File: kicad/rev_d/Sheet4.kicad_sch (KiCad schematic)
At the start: 22 parts, among them J2 JUMPER, J3 JUMPER, X7 DB15VGA, X8 PLB1-4I, X9 PLB1-2

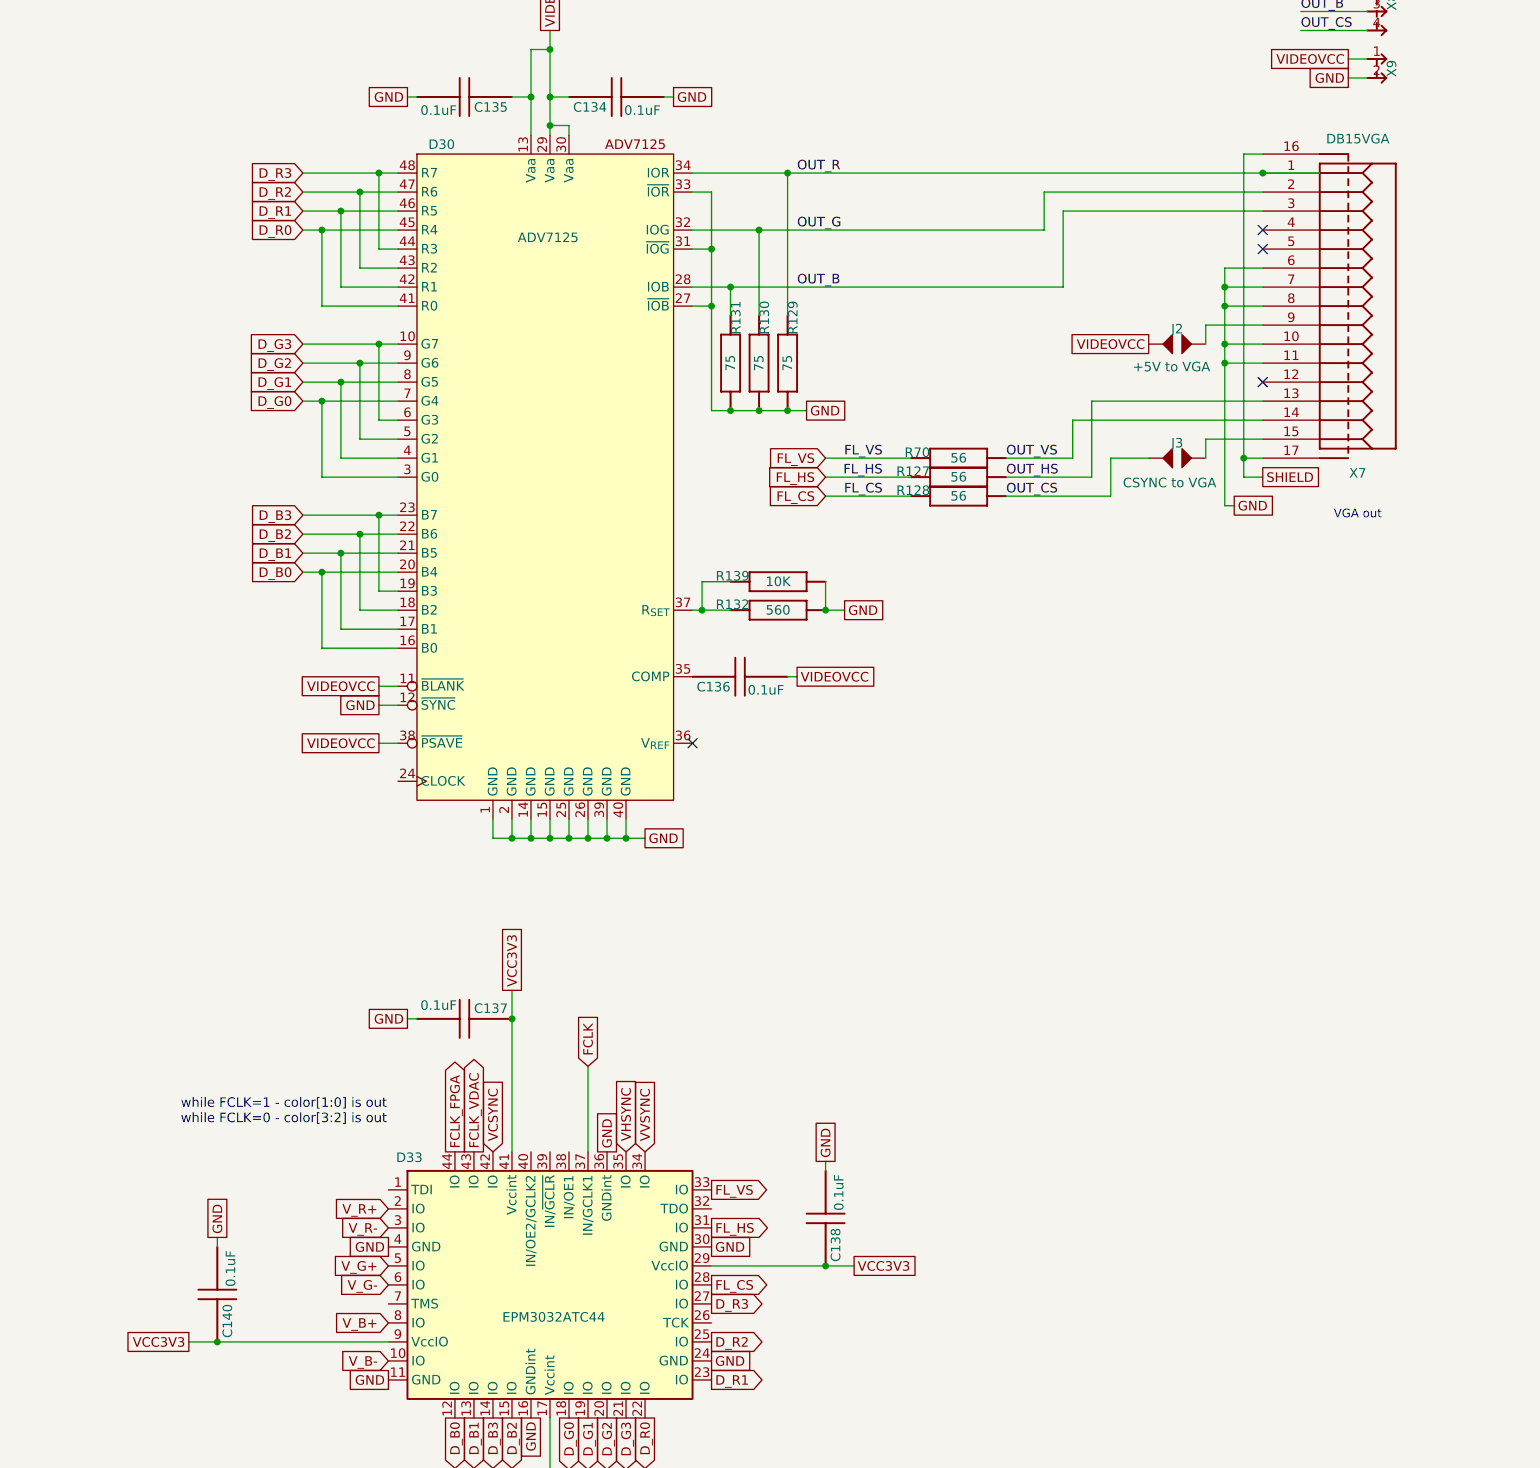
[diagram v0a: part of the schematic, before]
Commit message: pentevo: rev D: video output: remove 373/374 stuff (WIP); fix DA numbering issue
git-svn-id: svn://localhost/local-pentevo@1282 c6c76956-fad2-4150-a3a9-ea0a427205ba
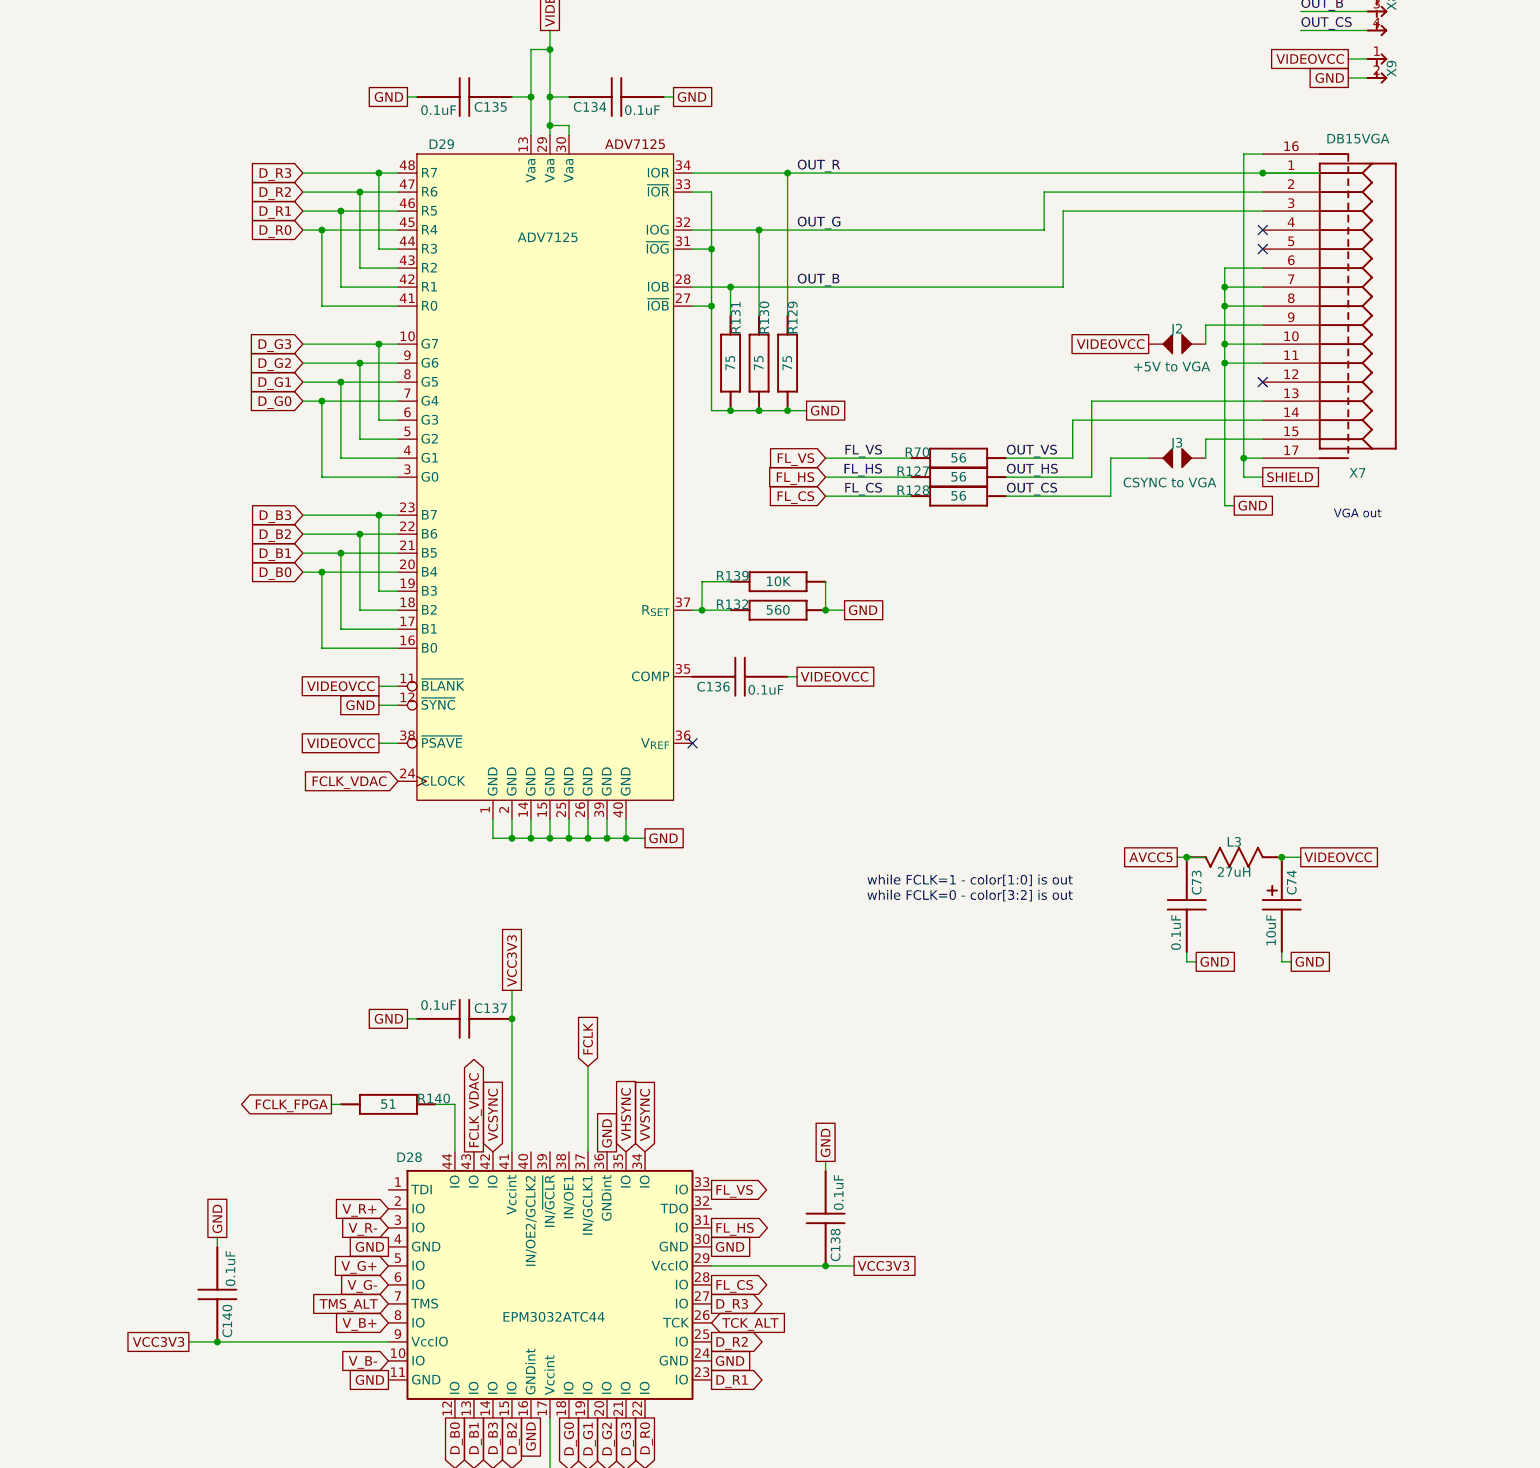
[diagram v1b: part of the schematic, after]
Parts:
- added C73: 0.1uF, C-CHIP, symbol eva-altium-import:Sheet1_3_CAPCHIP
- added C74: 10uF, EC-CHIP, symbol eva-altium-import:Sheet1_3_ECAPCHIP
- added L3: 27uH, CDR64B, symbol eva-altium-import:Sheet1_0_CDR64B
- added R140: 51, R-CHIP, symbol eva-altium-import:Sheet1_0_mirrored_RESCHIP
- renumbered D33 to D28, D30 to D29
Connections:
- net FCLK_FPGA: now also R140.1 (i/o); no longer D28.44 (IO)
- net FCLK_VDAC: now also D29.24 (CLOCK)
- net GND: now also C73.2, C74.2
- net VIDEOVCC: now also C74.1, L3.1
- net TCK_ALT: now reaches D28.26 (TCK)
- net TMS_ALT: now reaches D28.7 (TMS)
- new net: D28.44 (IO), R140.2 (i/o1)
- new net AVCC5: C73.1, L3.2

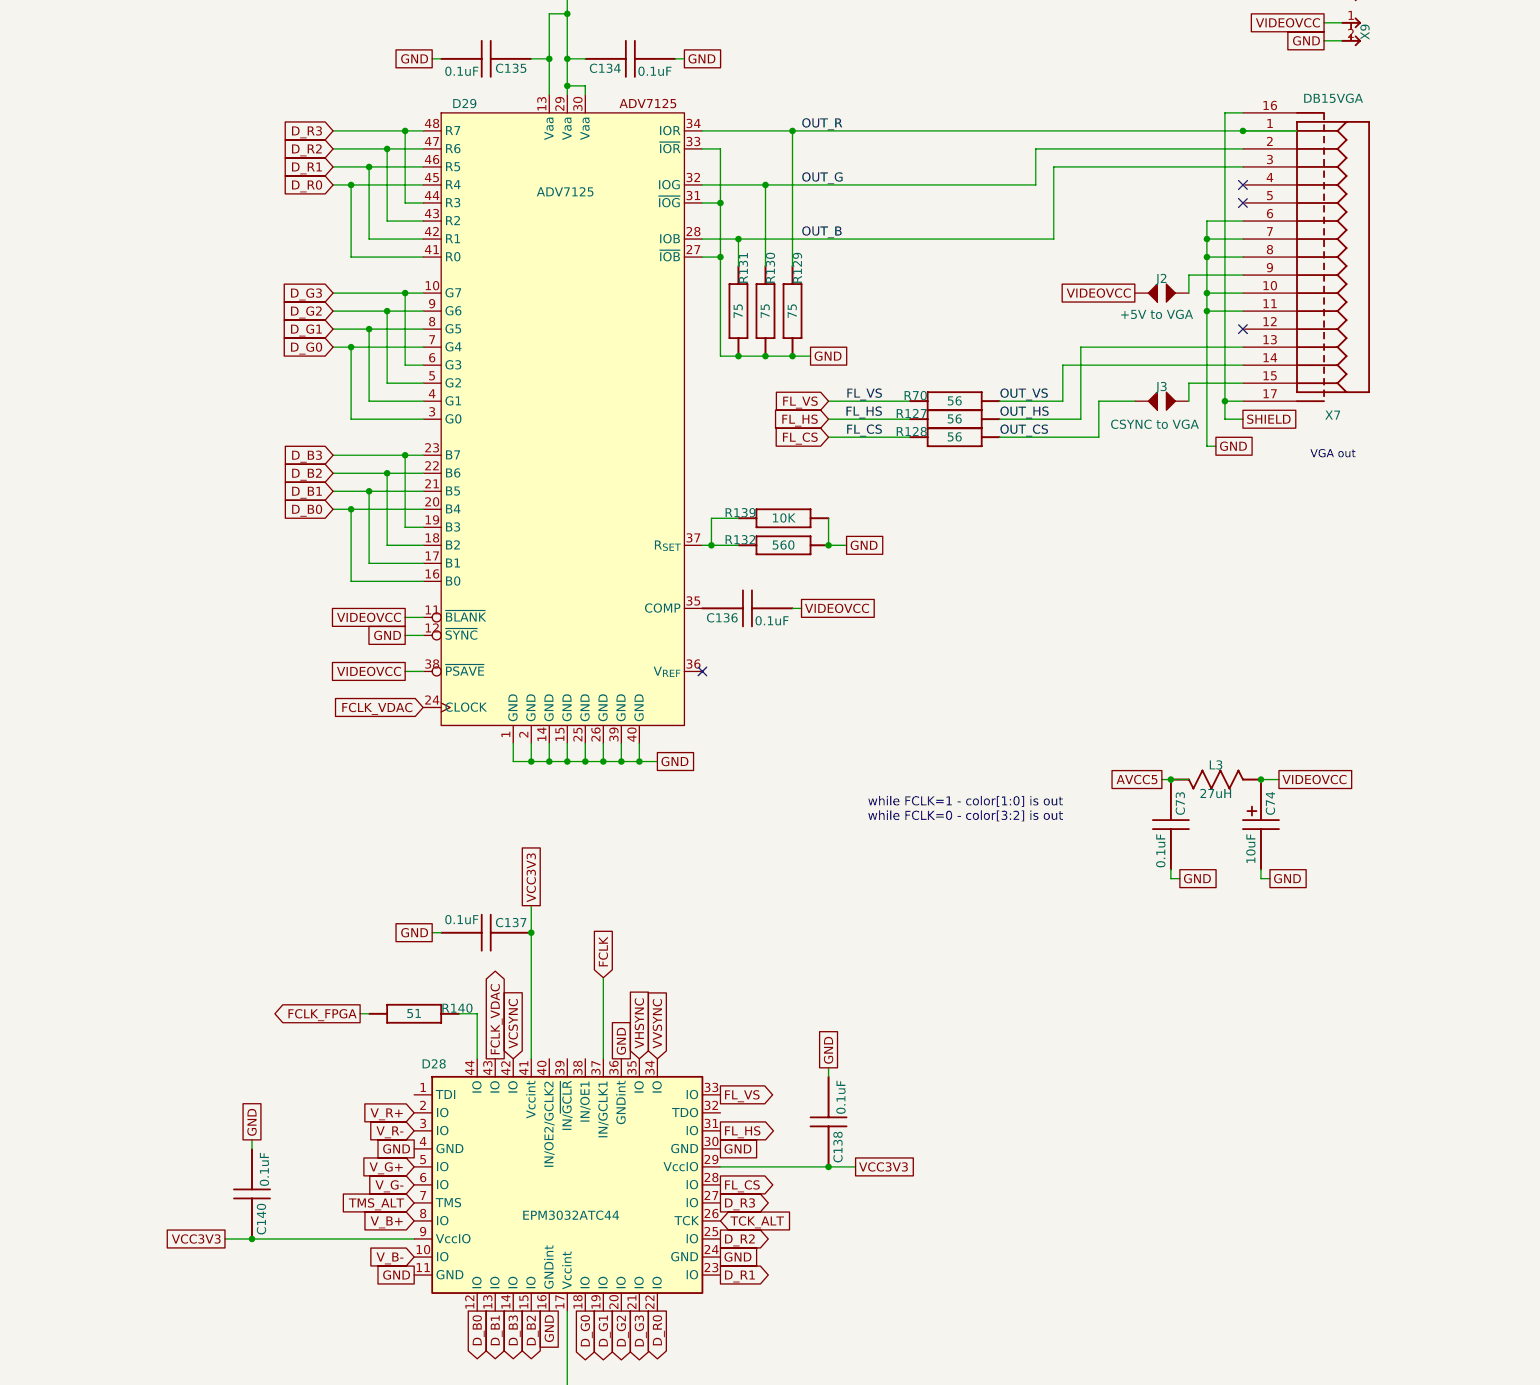
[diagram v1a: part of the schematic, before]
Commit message: pentevo: rev D: video output: add ext video/audio connector, set CPLD pins
git-svn-id: svn://localhost/local-pentevo@1283 c6c76956-fad2-4150-a3a9-ea0a427205ba
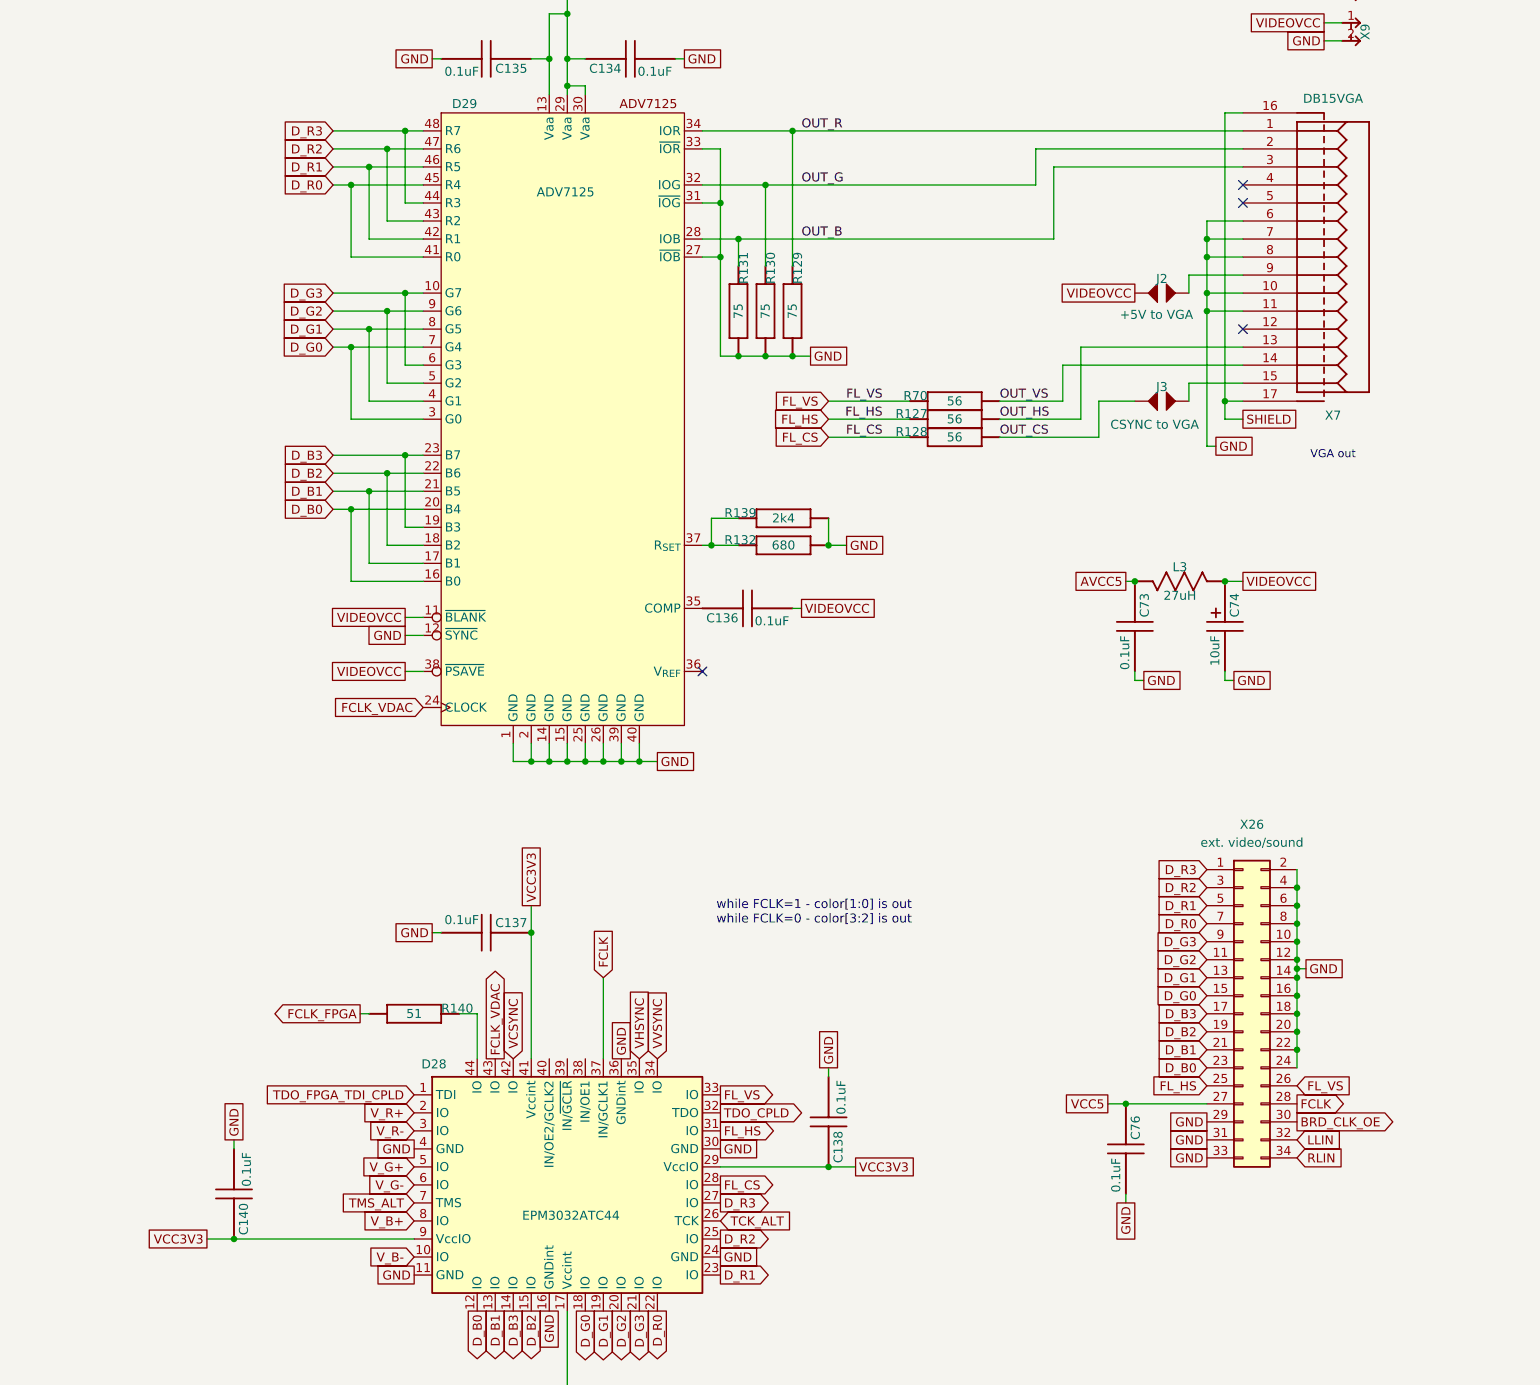
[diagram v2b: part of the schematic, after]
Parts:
- added C76: 0.1uF, C-CHIP, symbol eva-altium-import:Sheet1_3_CAPCHIP
- added X26: ext. video/sound, symbol Connector_Generic:Conn_02x17_Odd_Even
- R132: value 560 -> 680
- R139: value 10K -> 2k4
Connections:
- net D_B0: now also X26.23 (Pin_23)
- net D_B1: now also X26.21 (Pin_21)
- net D_B2: now also X26.19 (Pin_19)
- net D_B3: now also X26.17 (Pin_17)
- net D_G0: now also X26.15 (Pin_15)
- net D_G1: now also X26.13 (Pin_13)
- net D_G2: now also X26.11 (Pin_11)
- net D_G3: now also X26.9 (Pin_9)
- net D_R0: now also X26.7 (Pin_7)
- net D_R1: now also X26.5 (Pin_5)
- net D_R2: now also X26.3 (Pin_3)
- net D_R3: now also X26.1 (Pin_1)
- net FCLK: now also X26.28 (Pin_28)
- net FL_HS: now also X26.25 (Pin_25)
- net FL_VS: now also X26.26 (Pin_26)
- net GND: now also C76.2, X26.10 (Pin_10), X26.12 (Pin_12), X26.14 (Pin_14), X26.16 (Pin_16), X26.18 (Pin_18), X26.2 (Pin_2), X26.20 (Pin_20), X26.22 (Pin_22), X26.24 (Pin_24), X26.29 (Pin_29), X26.31 (Pin_31), X26.33 (Pin_33), X26.4 (Pin_4), X26.6 (Pin_6), X26.8 (Pin_8)
- net TDO_FPGA_TDI_CPLD: now reaches D28.1 (TDI)
- net TDO_CPLD: now reaches D28.32 (TDO)
- new net BRD_CLK_OE: X26.30 (Pin_30)
- new net LLIN: X26.32 (Pin_32)
- new net RLIN: X26.34 (Pin_34)
- new net VCC5: C76.1, X26.27 (Pin_27)
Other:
- moved on the sheet: C140, C73, C74, L3
